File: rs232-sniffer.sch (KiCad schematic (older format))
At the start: 45 parts, among them J101 DB9_Female, J102 Stiftleiste 2x9, J103 DB9_Male, J104 Stiftleiste 2x9, SW101 DIP-Switch 8, U101 AMS1117-3.3

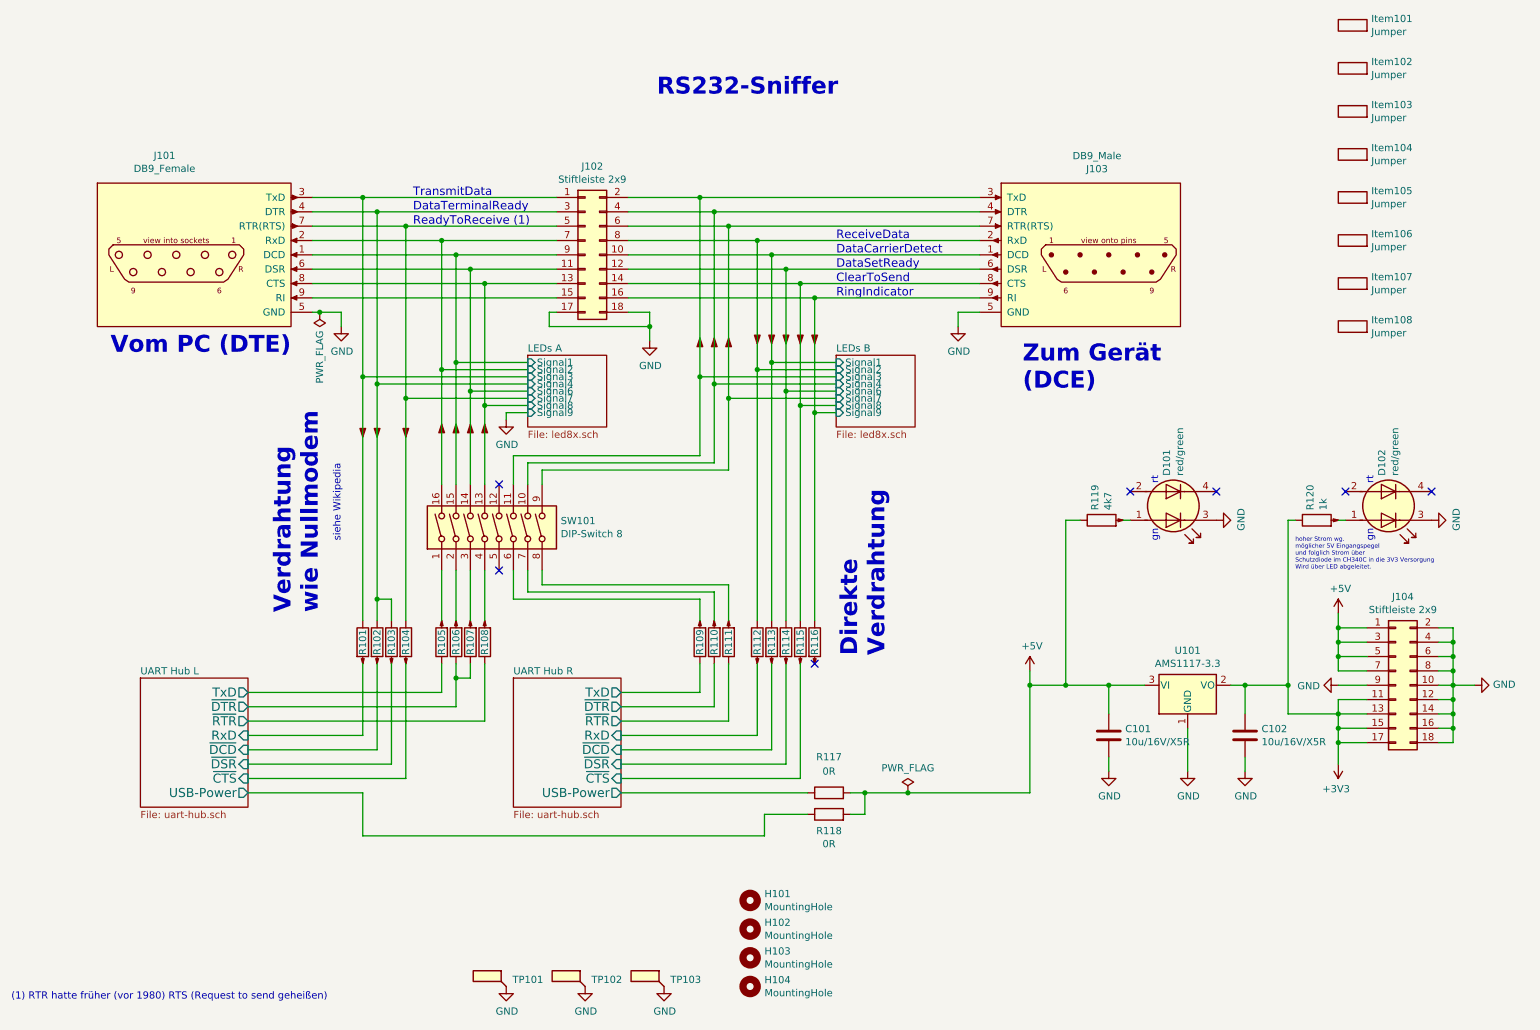
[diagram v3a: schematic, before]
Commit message: Layout fast fertig Footprint für 2x9-polig wurde aktualisiert
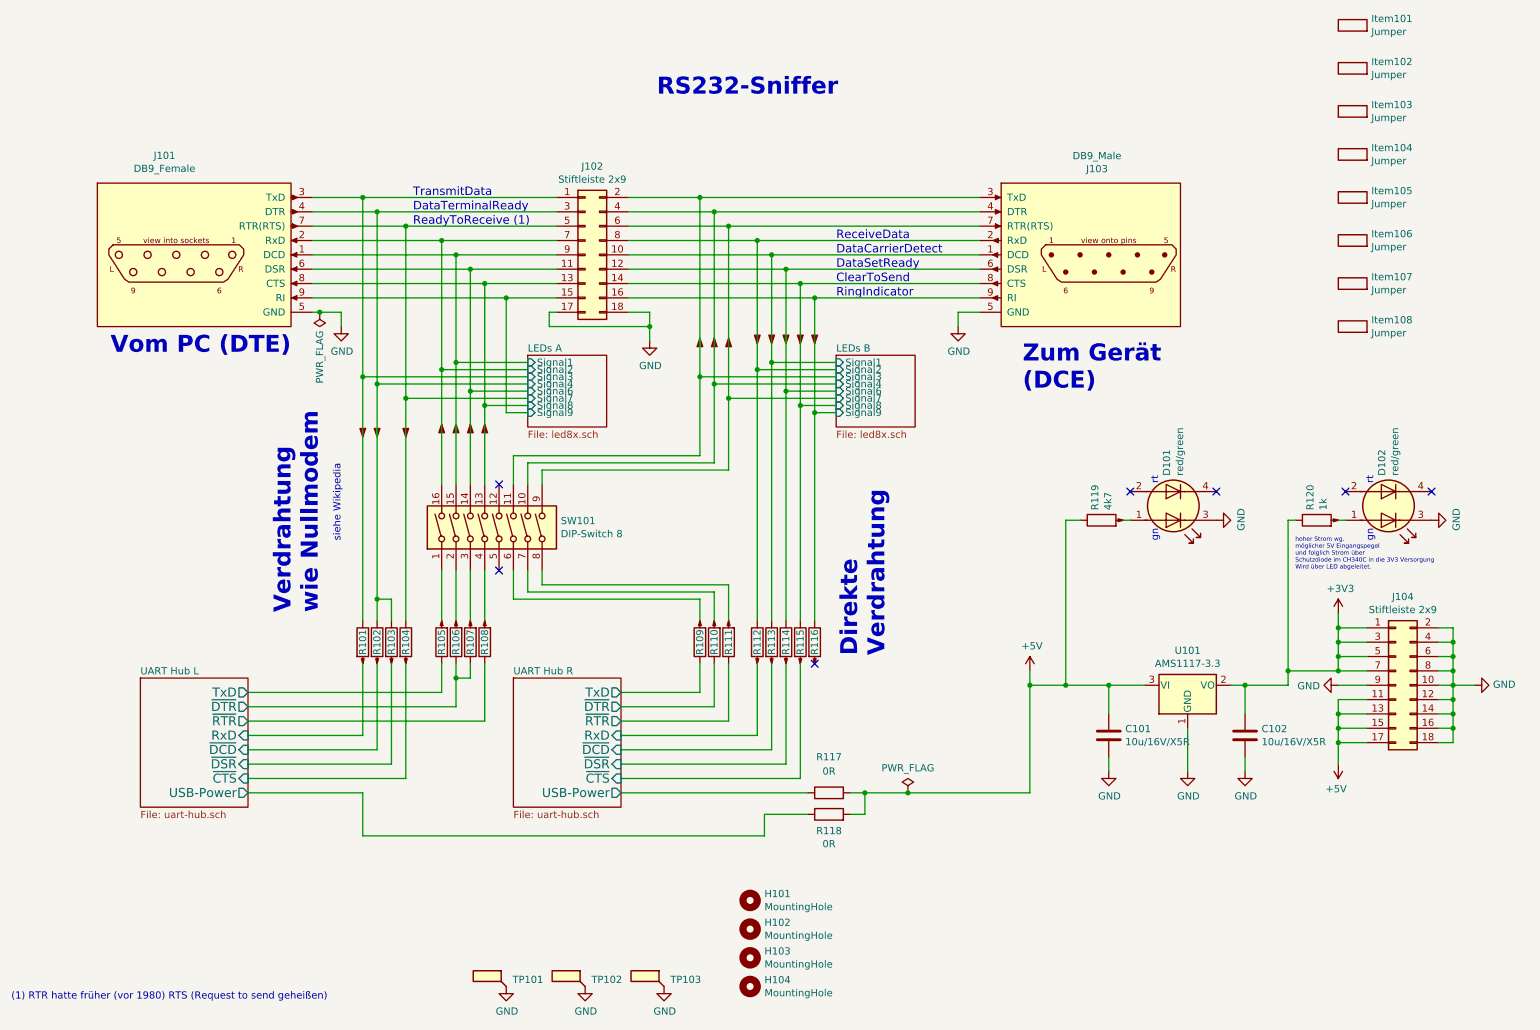
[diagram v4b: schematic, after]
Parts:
- J102, J104: footprint Connector_PinHeader_2.54mm:PinHeader_2x09_P2.54mm_Vertical_SMD -> htl_connectors:PinHeader_2x09_P2.54mm_Vertical_SMD_LCSC_C88175
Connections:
- net +3V3: now also J104.1 (Pin_1), J104.3 (Pin_3), J104.5 (Pin_5), J104.7 (Pin_7); no longer J104.11 (Pin_11), J104.13 (Pin_13), J104.15 (Pin_15), J104.17 (Pin_17)
- net +5V: now also J104.11 (Pin_11), J104.13 (Pin_13), J104.15 (Pin_15), J104.17 (Pin_17); no longer J104.1 (Pin_1), J104.3 (Pin_3), J104.5 (Pin_5), J104.7 (Pin_7)
- net LEDs A/Signal9: now reaches J101.9 (RI), J102.15 (Pin_15)
